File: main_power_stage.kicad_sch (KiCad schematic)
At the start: 69 parts, among them SW1 CAS-120TA, U2 LV14540DDAR, U6 TPS65987DDHRSHR, U7 LV14540DDAR, U8 74CBTLV3257_VQFN, U9 W25Q80DV_SOIC-8

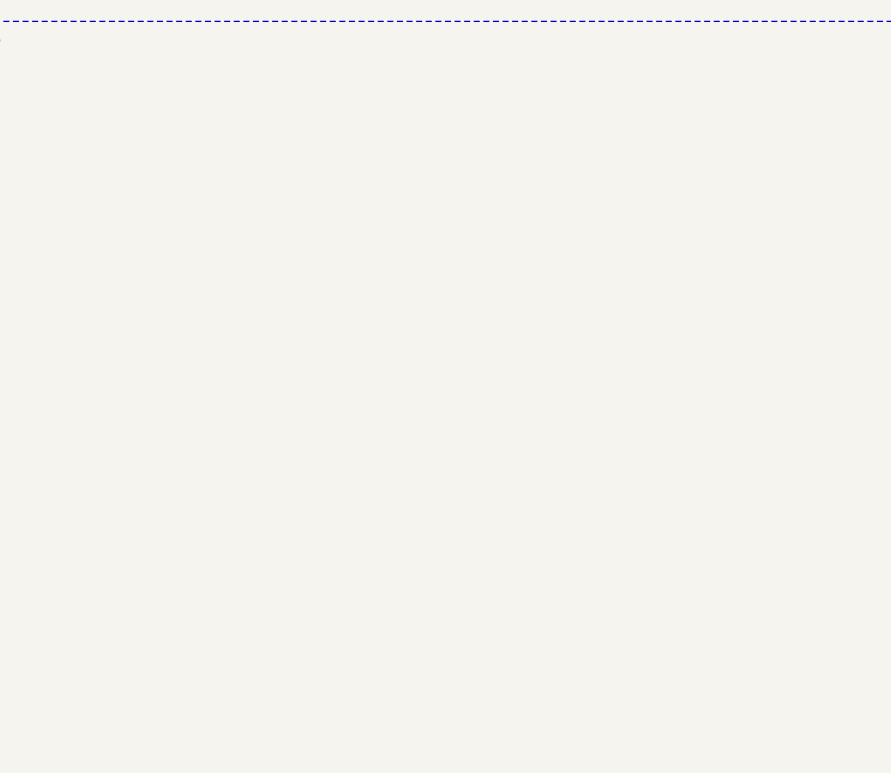
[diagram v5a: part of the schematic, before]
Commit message: [#62835] Add 3V3 LDO
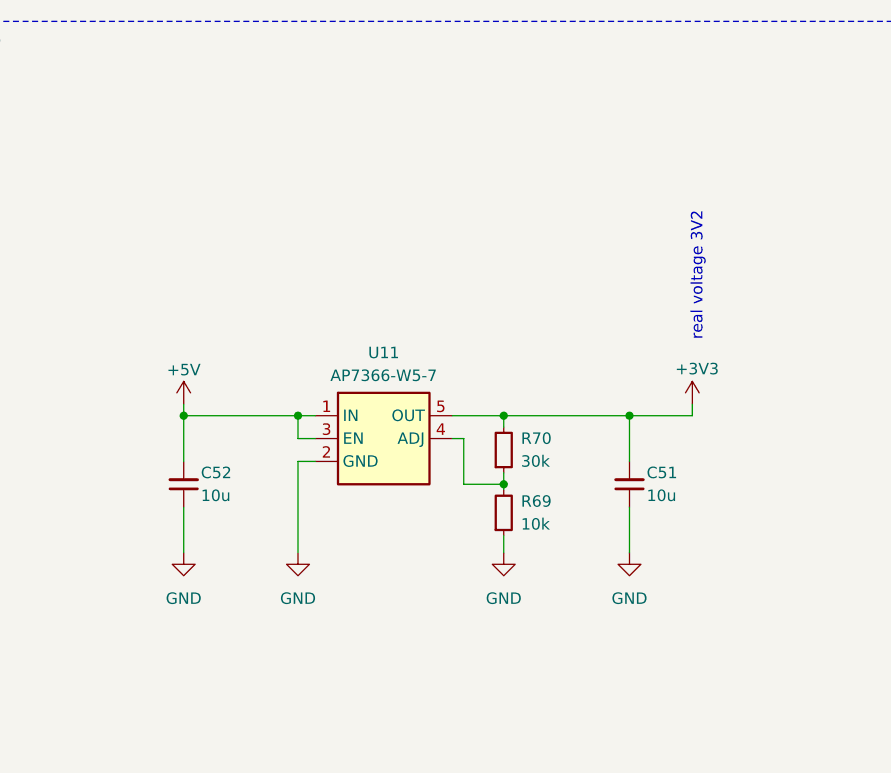
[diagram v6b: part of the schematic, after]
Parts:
- added C51, C52: C_10u_10V_0402, antmicro-footprints:C_0402_1005Metric, symbol antmicroCapacitors0402:C_10u_10V_0402
- added R69: R_10k_0402, antmicro-footprints:R_0402_1005Metric, symbol antmicroResistors0402:R_10k_0402
- added R70: R_30k_0402, antmicro-footprints:R_0402_1005Metric, symbol antmicroResistors0402:R_30k_0402
- added U11: AP7366_SOT, antmicro-footprints:SOT-23-5, symbol antmicroPMICVoltageRegulatorsLinear:AP7366_SOT
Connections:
- net +3V3: now also C51.2, R70.2, U11.5 (OUT)
- net +5V: now also C52.2, U11.1 (IN), U11.3 (EN)
- net GND: now also C51.1, C52.1, R69.1, U11.2 (GND)
- new net: R69.2, R70.1, U11.4 (ADJ)
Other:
- note added: "real voltage 3V2"

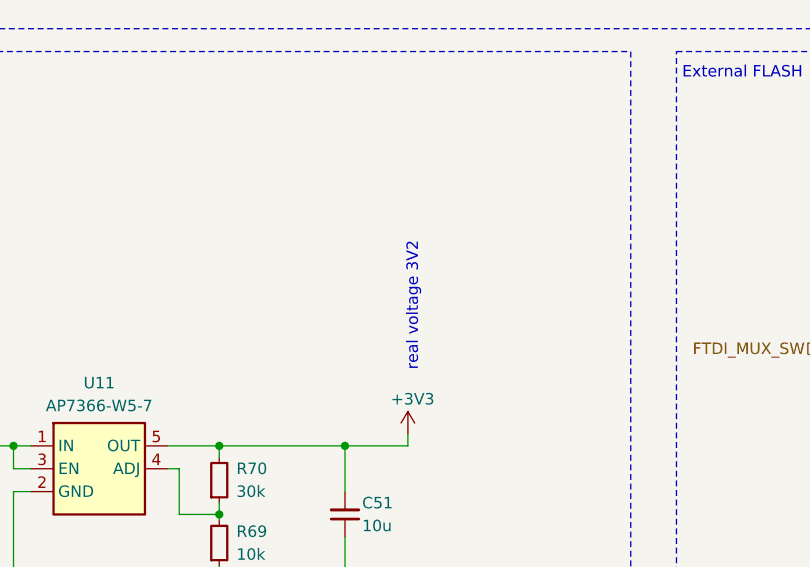
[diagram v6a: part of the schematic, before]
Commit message: [#62835] Add 3V3 LDO to PCB, place CBUS capacitors, change 5V buck layout
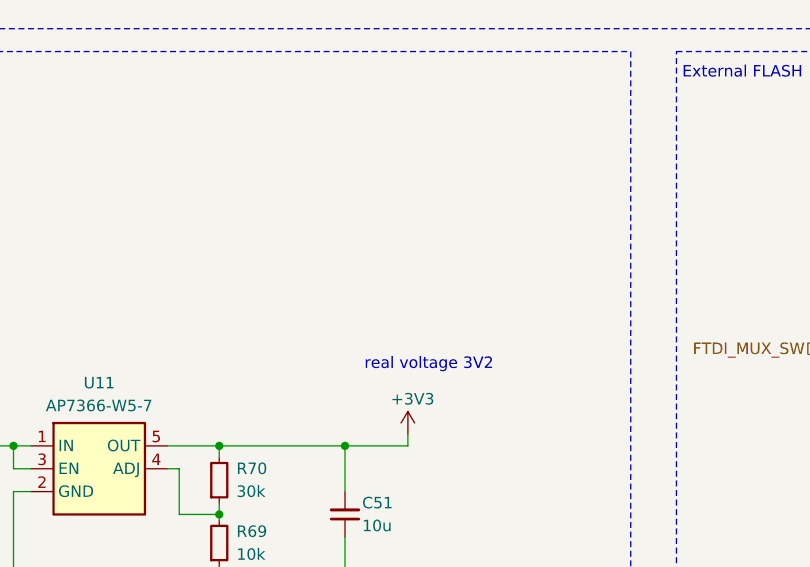
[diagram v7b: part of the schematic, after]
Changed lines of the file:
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@@
     (fill (type none))
   )
-  (text "real voltage 3V2" (at 100.33 224.79 90)
-    (effects (font (size 1.27 1.27)) (justify left bottom))
+  (text "real voltage 3V2" (at 108.585 224.79 0)
+    (effects (font (size 1.27 1.27)) (justify right bottom))
   )
   (text "External FLASH" (at 129.54 192.405 0)

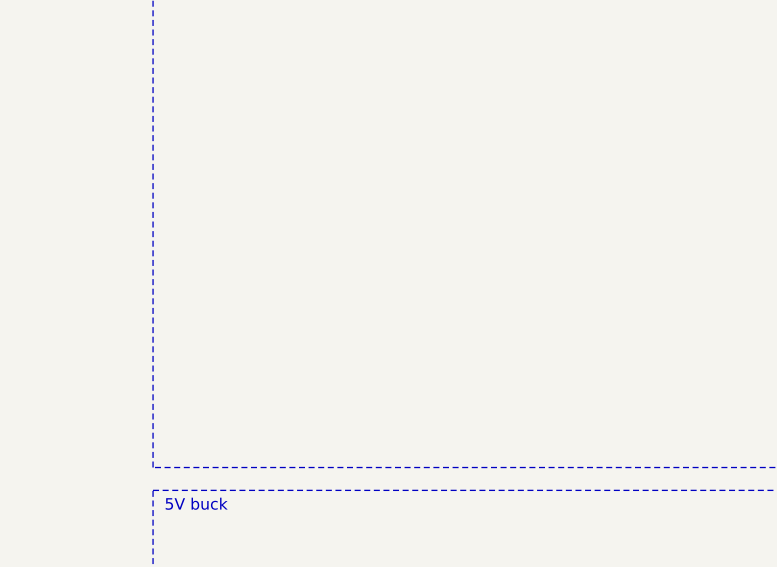
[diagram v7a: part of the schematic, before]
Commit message: [#63274] Add heatsink, start moving components to make space
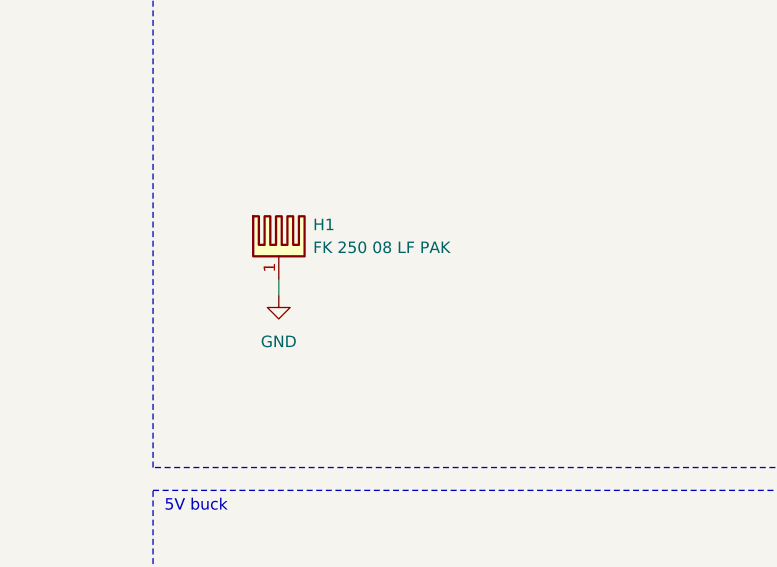
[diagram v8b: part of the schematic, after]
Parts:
- added H1: Heatsink_Fischer_FK250_08_LF_PAK_15x8mm, antmicro-footprints:Heatsink_Fischer_FK250_08_LF_PAK_15x8mm, symbol antmicroMechanicalParts:Heatsink_Fischer_FK250_08_LF_PAK_15x8mm
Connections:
- net GND: now also H1.1
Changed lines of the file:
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@@
     (stroke (width 0) (type default))
   )
+  (wire (pts (xy 27.94 92.075) (xy 27.94 93.98))
+    (stroke (width 0) (type default))
+  )
   (wire (pts (xy 73.66 154.94) (xy 73.66 153.67))
     (stroke (width 0) (type default))
@@
     )
   )
+  (symbol (lib_id "antmicroMechanicalParts:Heatsink_Fischer_FK250_08_LF_PAK_15x8mm") (at 27.94 92.075 0) (unit 1)
+    (in_bom yes) (on_board yes) (dnp no) (fields_autoplaced)
+    (property "Reference" "H1" (at 31.75 86.0679 0)
+      (effects (font (size 1.27 1.27) (thickness 0.15)) (justify left))
+    )
+    (property "Value" "Heatsink_Fischer_FK250_08_LF_PAK_15x8mm" (at 45.72 97.155 0)
+      (effects (font (size 1.27 1.27) (thickness 0.15)) (justify left bottom) hide)
+    )
+    (property "Footprint" "antmicro-footprints:Heatsink_Fischer_FK250_08_LF_PAK_15x8mm" (at 45.72 99.695 0)
+      (effects (font (size 1.27 1.27) (thickness 0.15)) (justify left bottom) hide)
+    )
+    (property "Datasheet" "https://www.tme.eu/Document/56bb1b034009250294cbf0606aed6e7b/FK%20250%2008%20LF%20PAK.pdf" (at 45.72 102.235 0)
+      (effects (font (size 1.27 1.27) (thickness 0.15)) (justify left bottom) hide)
+    )
+    (property "MPN" "FK 250 08 LF PAK" (at 31.75 88.6079 0)
+      (effects (font (size 1.27 1.27) (thickness 0.15)) (justify left))
+    )
+    (property "Manufacturer" "Fischer Elektronik" (at 45.72 104.775 0)
+      (effects (font (size 1.27 1.27) (thickness 0.15)) (justify left bottom) hide)
+    )
+    (property "Author" "Antmicro" (at 45.72 107.315 0)
+      (effects (font (size 1.27 1.27) (thickness 0.15)) (justify left bottom) hide)
+    )
+    (property "License" "Apache-2.0" (at 45.72 109.855 0)
+      (effects (font (size 1.27 1.27) (thickness 0.15)) (justify left bottom) hide)
+    )
+    (pin "1")
+    (instances
+      (project "antmicro-poe-to-usbc-pd-adapter"
+        (path "/cf0d4429-3f03-449f-96a7-26d69371a46d/47a421e3-70a1-4c86-94f4-557263ac6525"
+          (reference "H1") (unit 1)
+        )
+      )
+    )
+  )
   (symbol (lib_id "antmicroTestPoints:TP_0.75mm_SMD") (at 309.88 87.63 0) (unit 1)
     (in_bom no) (on_board yes) (dnp no) (fields_autoplaced)
@@
         )
       )
+    )
+  )
+  (symbol (lib_id "antmicropower:GND") (at 27.94 93.98 0) (unit 1)
+    (in_bom yes) (on_board yes) (dnp no) (fields_autoplaced)
+    (property "Reference" "#PWR0119" (at 36.83 96.52 0)
+      (effects (font (size 1.27 1.27) (thickness 0.15)) (justify left bottom) hide)
+    )
+    (property "Value" "GND" (at 27.94 99.06 0)
+      (effects (font (size 1.27 1.27) (thickness 0.15)))
+    )
+    (property "Footprint" "" (at 36.83 101.6 0)
+      (effects (font (size 1.27 1.27) (thickness 0.15)) (justify left bottom) hide)
+    )
+    (property "Datasheet" "" (at 36.83 106.68 0)
+      (effects (font (size 1.27 1.27) (thickness 0.15)) (justify left bottom) hide)
+    )
+    (property "Author" "Antmicro" (at 36.83 101.6 0)
+      (effects (font (size 1.27 1.27) (thickness 0.15)) (justify left bottom) hide)
+    )
+    (property "License" "Apache-2.0" (at 36.83 104.14 0)
+      (effects (font (size 1.27 1.27) (thickness 0.15)) (justify left bottom) hide)
+    )
+    (pin "1")
+    (instances
+      (project "antmicro-poe-to-usbc-pd-adapter"
+        (path "/cf0d4429-3f03-449f-96a7-26d69371a46d/47a421e3-70a1-4c86-94f4-557263ac6525"
+          (reference "#PWR0119") (unit 1)
+        )
+      )
